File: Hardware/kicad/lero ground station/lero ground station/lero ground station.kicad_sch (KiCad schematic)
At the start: 22 parts, among them J1 Screw_Terminal_01x02, J2 Conn_01x03, SW1 SW_Push_Dual, SW2 SW_Push_Dual, SW2 SW_Push_SPDT, SW3 SW_Push_Dual, SW4 SW_Push_Dual, SW5 SW_Push_Dual, U1 EBYTE_E22 XXXDXXT, U2 MAX98357A BREAKOUT, U3 Pico

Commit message: schemtic before soildering
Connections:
- net BCLK: now also U3.31 (GPIO26_ADC0); no longer U3.32 (GPIO27_ADC1)
- net BUT1: now also U3.27 (GPIO21); no longer U3.26 (GPIO20)
- net BUT2: now also U3.26 (GPIO20); no longer U3.27 (GPIO21)
- net BUT5: now also U3.12 (GPIO9); no longer U3.29 (GPIO22)
- net DIN: now also U3.29 (GPIO22); no longer U3.31 (GPIO26_ADC0)
- net GND: now also DS1.15 (~{CS1})
- net LRC: now also U3.32 (GPIO27_ADC1); no longer U3.34 (GPIO28_ADC2)
- net BATT_SENSE: now reaches R1.2, R2.1
- net BATT_SENSE: now also U3.34 (GPIO28_ADC2)
- no-connect marks 28 -> 30
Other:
- moved on the sheet: D1, U3

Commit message: schematic
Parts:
- R1: value 15k -> 20k
- R2: value 5k -> 20k
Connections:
- net BUT1: now also U3.8 (GND); no longer U3.27 (GPIO21)
- net BUT2: now also U3.9 (GPIO6); no longer U3.26 (GPIO20)
- net BUT3: now also U3.10 (GPIO7); no longer U3.25 (GPIO19)
- net BUT4: now also U3.11 (GPIO8); no longer U3.24 (GPIO18)
- no-connect marks 30 -> 26
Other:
- moved on the sheet: D1, U3

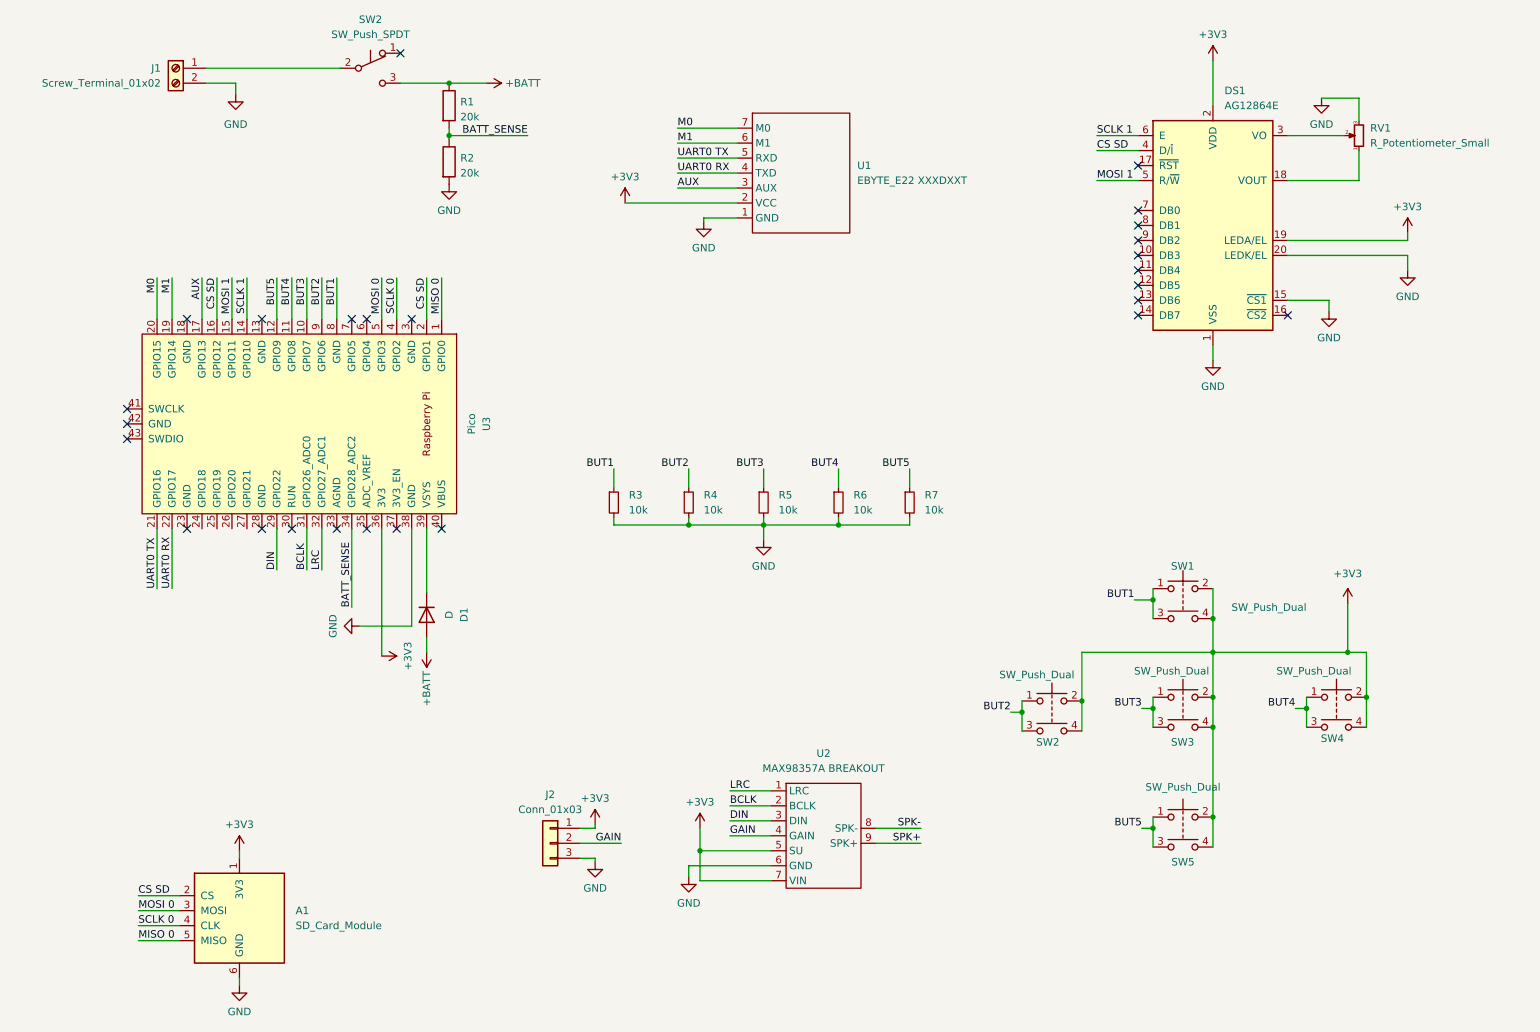
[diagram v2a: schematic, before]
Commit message: lcd kinda workign with nano
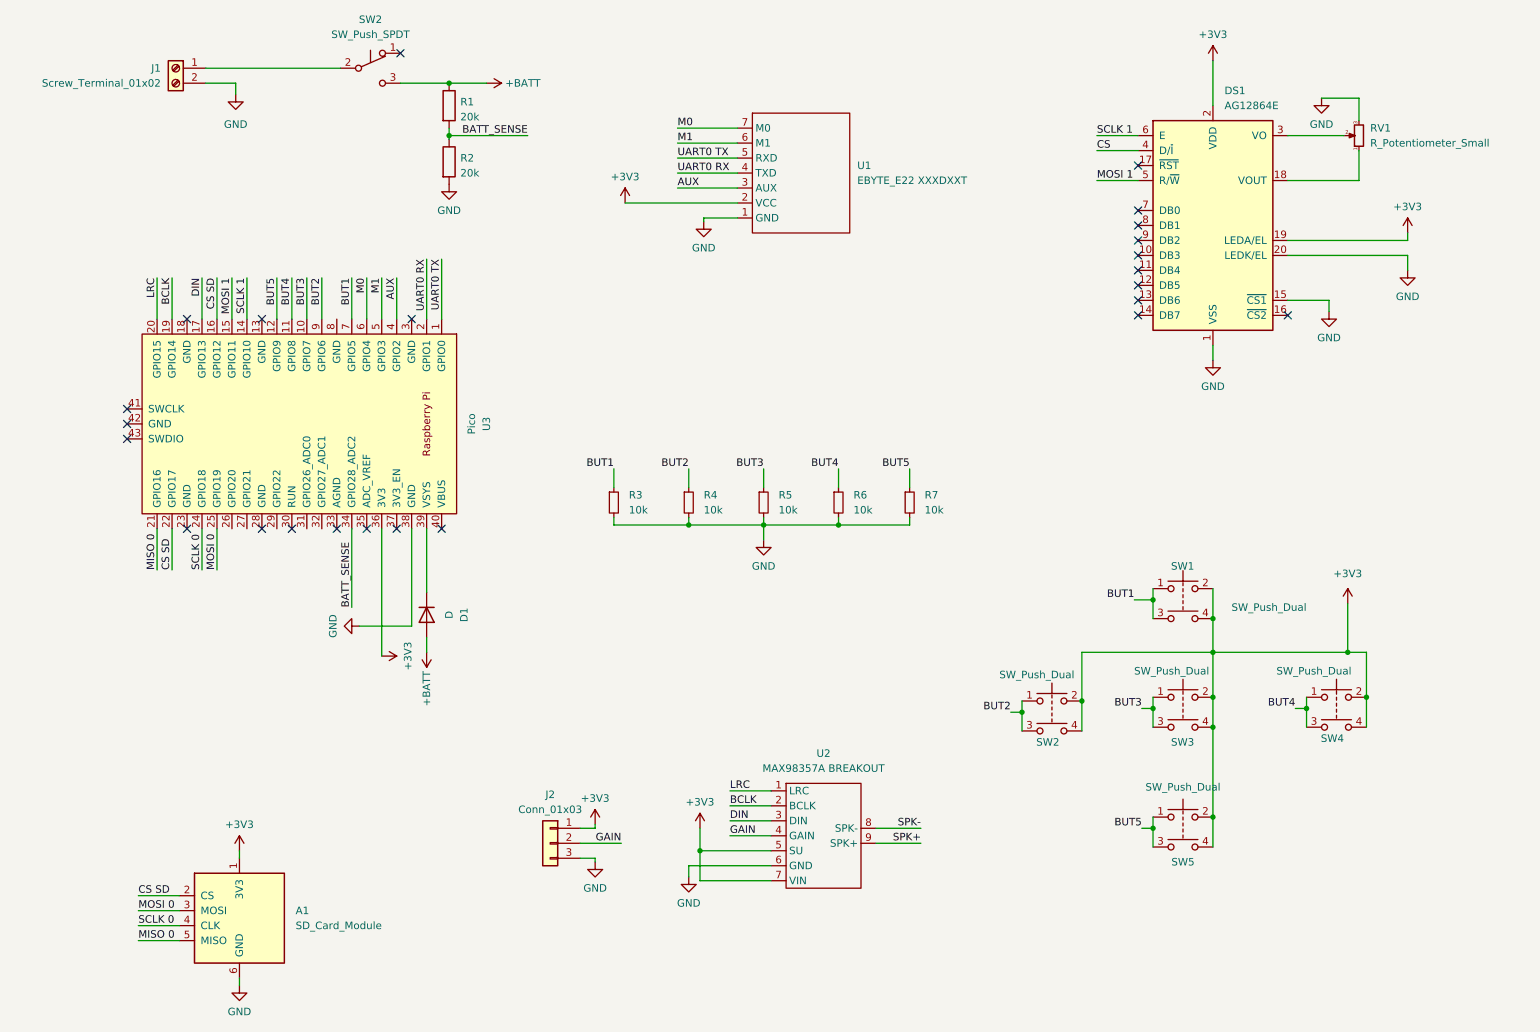
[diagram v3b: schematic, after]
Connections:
- net AUX: now also U3.4 (GPIO2); no longer U3.17 (GPIO13)
- net BCLK: now also U3.19 (GPIO14); no longer U3.31 (GPIO26_ADC0)
- net BUT1: now also U3.7 (GPIO5); no longer U3.8 (GND)
- net CS SD: now also U3.22 (GPIO17); no longer DS1.4 (D/~{I}), U3.2 (GPIO1)
- net DIN: now also U3.17 (GPIO13); no longer U3.29 (GPIO22)
- net LRC: now also U3.20 (GPIO15); no longer U3.32 (GPIO27_ADC1)
- net M0: now also U3.6 (GPIO4); no longer U3.20 (GPIO15)
- net M1: now also U3.5 (GPIO3); no longer U3.19 (GPIO14)
- net MISO 0: now also U3.21 (GPIO16); no longer U3.1 (GPIO0)
- net MOSI 0: now also U3.25 (GPIO19); no longer U3.5 (GPIO3)
- net SCLK 0: now also U3.24 (GPIO18); no longer U3.4 (GPIO2)
- net UART0 RX: now also U3.2 (GPIO1); no longer U3.22 (GPIO17)
- net UART0 TX: now also U3.1 (GPIO0); no longer U3.21 (GPIO16)
- new net CS: DS1.4 (D/~{I})
- no-connect marks 26 -> 24
